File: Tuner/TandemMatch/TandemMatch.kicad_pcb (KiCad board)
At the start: 2 copper layers, 100 x 100 mm, 124 parts, among them J1 Conn_01x02, J10 Conn_01x01, J11 Conn_01x01, J12 Conn_01x01, J13 Conn_01x01, J14 Conn_01x01, J15 Conn_01x01, J16 Conn_01x01, J17 Conn_01x02, J18 Conn_Coaxial, J19 Conn_01x02, J2 Conn_01x02, J20 Conn_Coaxial, J21 Conn_01x01, J22 Conn_01x01, J23 Conn_01x01, J24 Conn_01x01, J25 Conn_01x01, J26 Conn_01x01, J27 Conn_01x01, J28 Conn_01x01, J29 Conn_01x01, J3 Conn_Coaxial, J30 Conn_01x01, J31 Conn_01x01, J32 Conn_01x01, J33 Conn_01x03, J34 Conn_01x01, J35 Conn_01x01, J36 Conn_01x01, J37 Conn_01x01, J38 Conn_01x01, J39 Conn_01x01, J4 Conn_Coaxial, J40 Conn_01x01, J41 Conn_01x01, J42 Conn_01x01, J43 Conn_01x02, J44 Conn_Coaxial, J45 Conn_01x01, J46 Conn_01x01, J47 Conn_01x01, J48 Conn_01x01, J49 Conn_01x01, J5 Conn_01x01, J50 Conn_01x01, J51 Conn_01x01, J52 Conn_01x01, J53 Conn_01x01, J54 Conn_01x02, J55 Conn_01x01, J56 Conn_01x01, J57 Conn_01x01, J58 Conn_01x02, J59 Conn_Coaxial, J6 Conn_01x01, J60 Conn_01x01, J61 Conn_01x01, J62 Conn_01x01, J63 Conn_01x01, J64 Conn_01x01, J65 Conn_01x01, J66 Conn_01x01, J67 Conn_01x01, J68 Conn_01x02, J69 Conn_01x01, J7 Conn_01x01, J70 Conn_01x01, J71 Conn_01x01, J72 Conn_01x01, J73 Conn_01x01, J74 Conn_01x02, J75 Conn_01x02, J76 Conn_01x02, J77 Conn_01x01, J78 Conn_01x01, J79 Conn_01x01, J8 Conn_01x01, J80 Conn_01x01, J81 Conn_01x01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

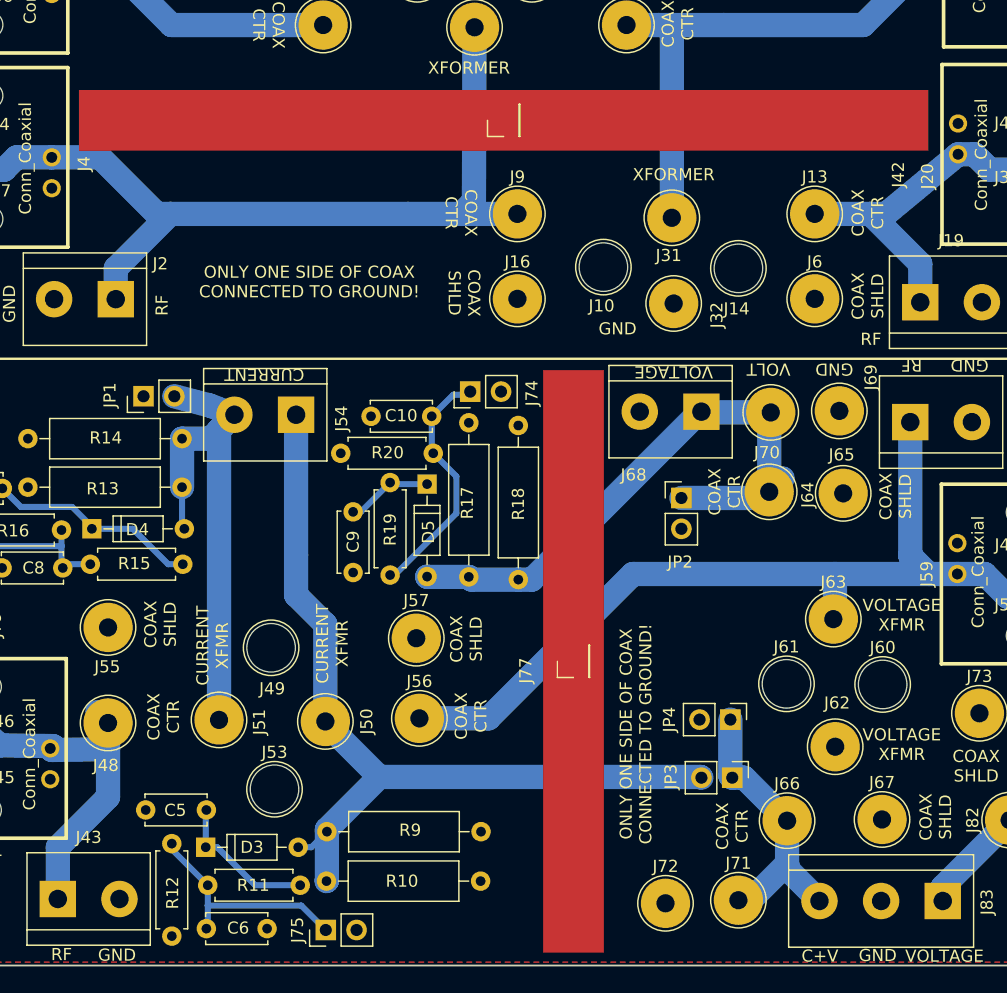
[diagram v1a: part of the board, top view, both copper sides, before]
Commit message: Fixed TandemMatch grounding problem
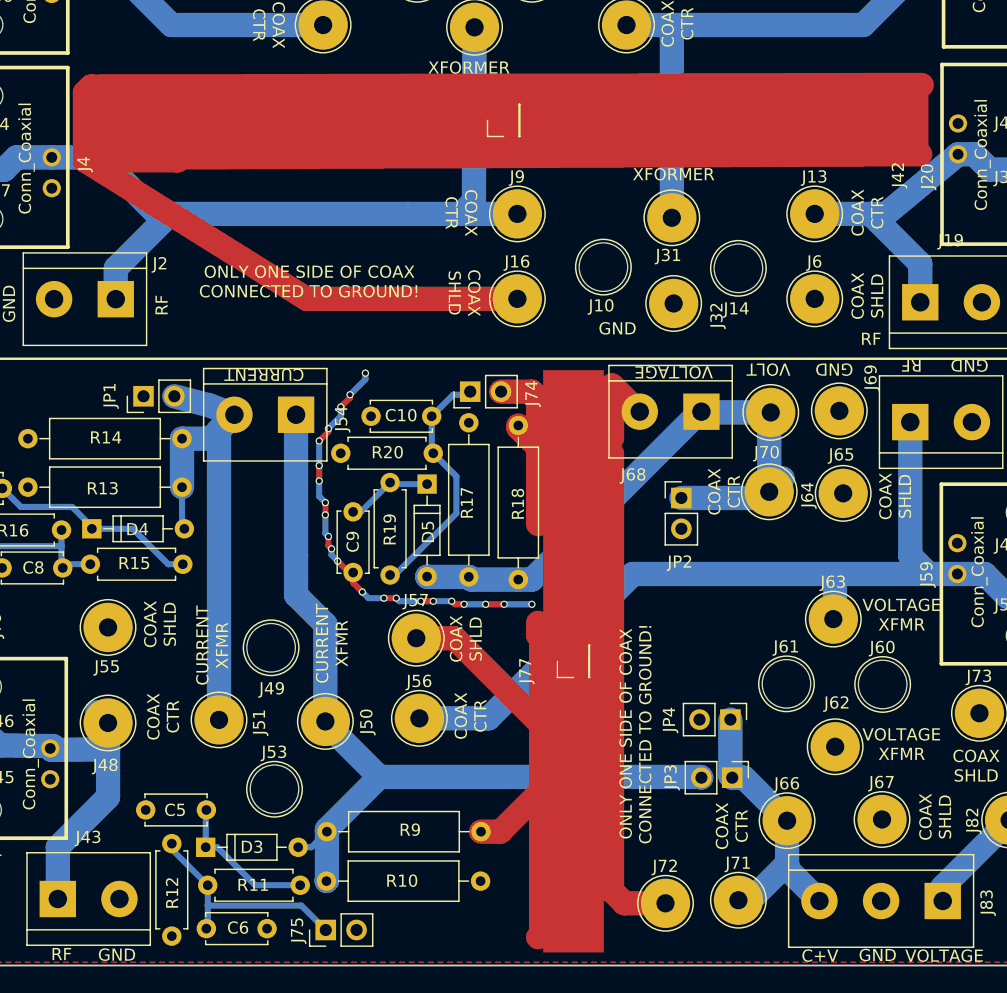
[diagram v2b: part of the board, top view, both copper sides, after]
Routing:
- net GND: track 0.00 -> 336.9 mm, vias 0 -> 22
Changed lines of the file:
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@@
     (links 149)
     (no_connects 0)
-    (area 18.581999 37.92438 161.377001 141.821259)
+    (area 39.924999 39.924999 140.075001 140.075001)
     (thickness 1.6)
     (drawings 65)
-    (tracks 204)
+    (tracks 294)
     (zones 0)
     (modules 124)
@@
   (segment (start 62.5 62.5) (end 57.404 57.404) (width 2) (layer B.Cu) (net 1))
   (segment (start 52.735 57.5) (end 52.639 57.404) (width 2) (layer B.Cu) (net 1) (status 30))
+  (segment (start 89.662 92.71) (end 92.202 92.71) (width 2) (layer F.Cu) (net 2))
+  (segment (start 92.71 93.218) (end 92.71 97.282) (width 2) (layer F.Cu) (net 2))
+  (segment (start 92.202 92.71) (end 92.71 93.218) (width 2) (layer F.Cu) (net 2))
+  (segment (start 92.71 97.282) (end 92.71 96.012) (width 2) (layer F.Cu) (net 2))
+  (segment (start 92.71 96.012) (end 92.71 97.282) (width 2) (layer F.Cu) (net 2))
+  (segment (start 101.092 94.361) (end 100.965 94.361) (width 2) (layer F.Cu) (net 2))
+  (segment (start 100.965 94.361) (end 98.806 92.202) (width 2) (layer F.Cu) (net 2))
+  (segment (start 98.806 92.202) (end 98.806 96.52) (width 2) (layer F.Cu) (net 2))
+  (segment (start 98.806 96.52) (end 98.552 96.774) (width 2) (layer F.Cu) (net 2))
+  (segment (start 82.677 113.03) (end 85.852 113.03) (width 2) (layer F.Cu) (net 2))
+  (segment (start 92.964 137.414) (end 92.71 137.668) (width 2) (layer F.Cu) (net 2))
+  (segment (start 92.964 120.142) (end 92.964 137.414) (width 2) (layer F.Cu) (net 2))
+  (segment (start 85.852 113.03) (end 92.964 120.142) (width 2) (layer F.Cu) (net 2))
+  (segment (start 91.0844 95.49892) (end 91.0844 95.6564) (width 2) (layer F.Cu) (net 2))
+  (segment (start 91.0844 95.6564) (end 92.71 97.282) (width 2) (layer F.Cu) (net 2))
+  (segment (start 92.71 97.282) (end 92.71 97.282) (width 2) (layer F.Cu) (net 2))
+  (segment (start 92.71 97.282) (end 92.71 103.632) (width 2) (layer F.Cu) (net 2))
+  (segment (start 88.011 128.97104) (end 89.60104 128.97104) (width 2) (layer F.Cu) (net 2))
+  (segment (start 92.71 112.776) (end 92.71 111.76) (width 2) (layer F.Cu) (net 2))
+  (segment (start 92.964 113.03) (end 92.71 112.776) (width 2) (layer F.Cu) (net 2))
+  (segment (start 92.964 125.60808) (end 92.964 113.03) (width 2) (layer F.Cu) (net 2))
+  (segment (start 89.60104 128.97104) (end 92.964 125.60808) (width 2) (layer F.Cu) (net 2))
+  (segment (start 103.2129 134.874) (end 99.822 134.874) (width 2) (layer F.Cu) (net 2))
+  (segment (start 98.806 133.858) (end 98.806 97.79) (width 2) (layer F.Cu) (net 2))
+  (segment (start 99.822 134.874) (end 98.806 133.858) (width 2) (layer F.Cu) (net 2))
+  (segment (start 55.372 73.66) (end 55.372 68.072) (width 2) (layer F.Cu) (net 2))
+  (segment (start 55.372 68.072) (end 55.88 67.564) (width 2) (layer F.Cu) (net 2))
+  (segment (start 55.88 67.564) (end 124.333 67.437) (width 2) (layer F.Cu) (net 2))
+  (segment (start 91.008 85.064) (end 73.634 85.064) (width 2) (layer F.Cu) (net 2))
+  (segment (start 63.246 73.406) (end 124.206 73.152) (width 2) (layer F.Cu) (net 2))
+  (segment (start 62.992 73.66) (end 63.246 73.406) (width 2) (layer F.Cu) (net 2))
+  (segment (start 55.372 73.66) (end 62.992 73.66) (width 2) (layer F.Cu) (net 2))
+  (segment (start 73.634 85.064) (end 55.372 73.66) (width 2) (layer F.Cu) (net 2))
+  (segment (start 77.47 107.616) (end 77.136 107.616) (width 0.5) (layer F.Cu) (net 2))
+  (segment (start 77.136 107.616) (end 76.2 106.68) (width 0.5) (layer F.Cu) (net 2))
+  (via (at 78.486 91.186) (size 0.6) (drill 0.4) (layers F.Cu B.Cu) (net 2))
+  (segment (start 78.486 91.694) (end 78.486 91.186) (width 0.5) (layer B.Cu) (net 2))
+  (segment (start 77.216 92.964) (end 78.486 91.694) (width 0.5) (layer B.Cu) (net 2))
+  (via (at 77.216 92.964) (size 0.6) (drill 0.4) (layers F.Cu B.Cu) (net 2))
+  (segment (start 77.216 93.218) (end 77.216 92.964) (width 0.5) (layer F.Cu) (net 2))
+  (segment (start 76.454 93.98) (end 77.216 93.218) (width 0.5) (layer F.Cu) (net 2))
+  (via (at 76.454 93.98) (size 0.6) (drill 0.4) (layers F.Cu B.Cu) (net 2))
+  (segment (start 76.454 94.742) (end 76.454 93.98) (width 0.5) (layer B.Cu) (net 2))
+  (segment (start 75.438 95.758) (end 76.454 94.742) (width 0.5) (layer B.Cu) (net 2))
+  (via (at 75.438 95.758) (size 0.6) (drill 0.4) (layers F.Cu B.Cu) (net 2))
+  (segment (start 75.438 96.012) (end 75.438 95.758) (width 0.5) (layer F.Cu) (net 2))
+  (segment (start 74.676 96.774) (end 75.438 96.012) (width 0.5) (layer F.Cu) (net 2))
+  (via (at 74.676 96.774) (size 0.6) (drill 0.4) (layers F.Cu B.Cu) (net 2))
+  (segment (start 74.676 98.806) (end 74.676 96.774) (width 0.5) (layer B.Cu) (net 2))
+  (via (at 74.676 98.806) (size 0.6) (drill 0.4) (layers F.Cu B.Cu) (net 2))
+  (segment (start 74.676 100.076) (end 74.676 98.806) (width 0.5) (layer F.Cu) (net 2))
+  (via (at 74.676 100.076) (size 0.6) (drill 0.4) (layers F.Cu B.Cu) (net 2))
+  (segment (start 74.676 101.346) (end 74.676 100.076) (width 0.5) (layer B.Cu) (net 2))
+  (segment (start 75.184 101.854) (end 74.676 101.346) (width 0.5) (layer B.Cu) (net 2))
+  (via (at 75.184 101.854) (size 0.6) (drill 0.4) (layers F.Cu B.Cu) (net 2))
+  (segment (start 75.184 102.87) (end 75.184 101.854) (width 0.5) (layer F.Cu) (net 2))
+  (via (at 75.184 102.87) (size 0.6) (drill 0.4) (layers F.Cu B.Cu) (net 2))
+  (segment (start 75.184 104.394) (end 75.184 102.87) (width 0.5) (layer B.Cu) (net 2))
+  (segment (start 75.438 104.648) (end 75.184 104.394) (width 0.5) (layer B.Cu) (net 2))
+  (via (at 75.438 104.648) (size 0.6) (drill 0.4) (layers F.Cu B.Cu) (net 2))
+  (segment (start 75.438 105.41) (end 75.438 104.648) (width 0.5) (layer F.Cu) (net 2))
+  (segment (start 75.692 105.664) (end 75.438 105.41) (width 0.5) (layer F.Cu) (net 2))
+  (via (at 75.692 105.664) (size 0.6) (drill 0.4) (layers F.Cu B.Cu) (net 2))
+  (segment (start 75.692 106.172) (end 75.692 105.664) (width 0.5) (layer B.Cu) (net 2))
+  (segment (start 76.2 106.68) (end 75.692 106.172) (width 0.5) (layer B.Cu) (net 2))
+  (via (at 76.2 106.68) (size 0.6) (drill 0.4) (layers F.Cu B.Cu) (net 2))
+  (segment (start 77.47 107.616) (end 77.47 108.458) (width 0.5) (layer F.Cu) (net 2))
+  (via (at 92.202 110.236) (size 0.6) (drill 0.4) (layers F.Cu B.Cu) (net 2))
+  (segment (start 89.916 110.236) (end 92.202 110.236) (width 0.5) (layer B.Cu) (net 2))
+  (via (at 89.916 110.236) (size 0.6) (drill 0.4) (layers F.Cu B.Cu) (net 2))
+  (segment (start 88.392 110.236) (end 89.916 110.236) (width 0.5) (layer F.Cu) (net 2))
+  (via (at 88.392 110.236) (size 0.6) (drill 0.4) (layers F.Cu B.Cu) (net 2))
+  (segment (start 86.614 110.236) (end 88.392 110.236) (width 0.5) (layer B.Cu) (net 2))
+  (via (at 86.614 110.236) (size 0.6) (drill 0.4) (layers F.Cu B.Cu) (net 2))
+  (segment (start 85.852 110.236) (end 86.614 110.236) (width 0.5) (layer F.Cu) (net 2))
+  (segment (start 85.598 109.982) (end 85.852 110.236) (width 0.5) (layer F.Cu) (net 2))
+  (via (at 85.598 109.982) (size 0.6) (drill 0.4) (layers F.Cu B.Cu) (net 2))
+  (segment (start 84.074 109.982) (end 85.598 109.982) (width 0.5) (layer B.Cu) (net 2))
+  (via (at 84.074 109.982) (size 0.6) (drill 0.4) (layers F.Cu B.Cu) (net 2))
+  (segment (start 83.058 109.982) (end 84.074 109.982) (width 0.5) (layer F.Cu) (net 2))
+  (via (at 83.058 109.982) (size 0.6) (drill 0.4) (layers F.Cu B.Cu) (net 2))
+  (segment (start 81.28 109.982) (end 83.058 109.982) (width 0.5) (layer B.Cu) (net 2))
+  (segment (start 81.026 109.728) (end 81.28 109.982) (width 0.5) (layer B.Cu) (net 2))
+  (via (at 81.026 109.728) (size 0.6) (drill 0.4) (layers F.Cu B.Cu) (net 2))
+  (segment (start 80.01 109.728) (end 81.026 109.728) (width 0.5) (layer F.Cu) (net 2))
+  (via (at 80.01 109.728) (size 0.6) (drill 0.4) (layers F.Cu B.Cu) (net 2))
+  (segment (start 78.74 109.728) (end 80.01 109.728) (width 0.5) (layer B.Cu) (net 2))
+  (segment (start 78.232 109.22) (end 78.74 109.728) (width 0.5) (layer B.Cu) (net 2))
+  (via (at 78.232 109.22) (size 0.6) (drill 0.4) (layers F.Cu B.Cu) (net 2))
+  (segment (start 77.47 108.458) (end 78.232 109.22) (width 0.5) (layer F.Cu) (net 2))
   (segment (start 87.4776 62.6872) (end 87.4268 77.0128) (width 2) (layer B.Cu) (net 3) (status 10))
   (segment (start 87.4268 77.0128) (end 86.3756 78.064) (width 2) (layer B.Cu) (net 3))

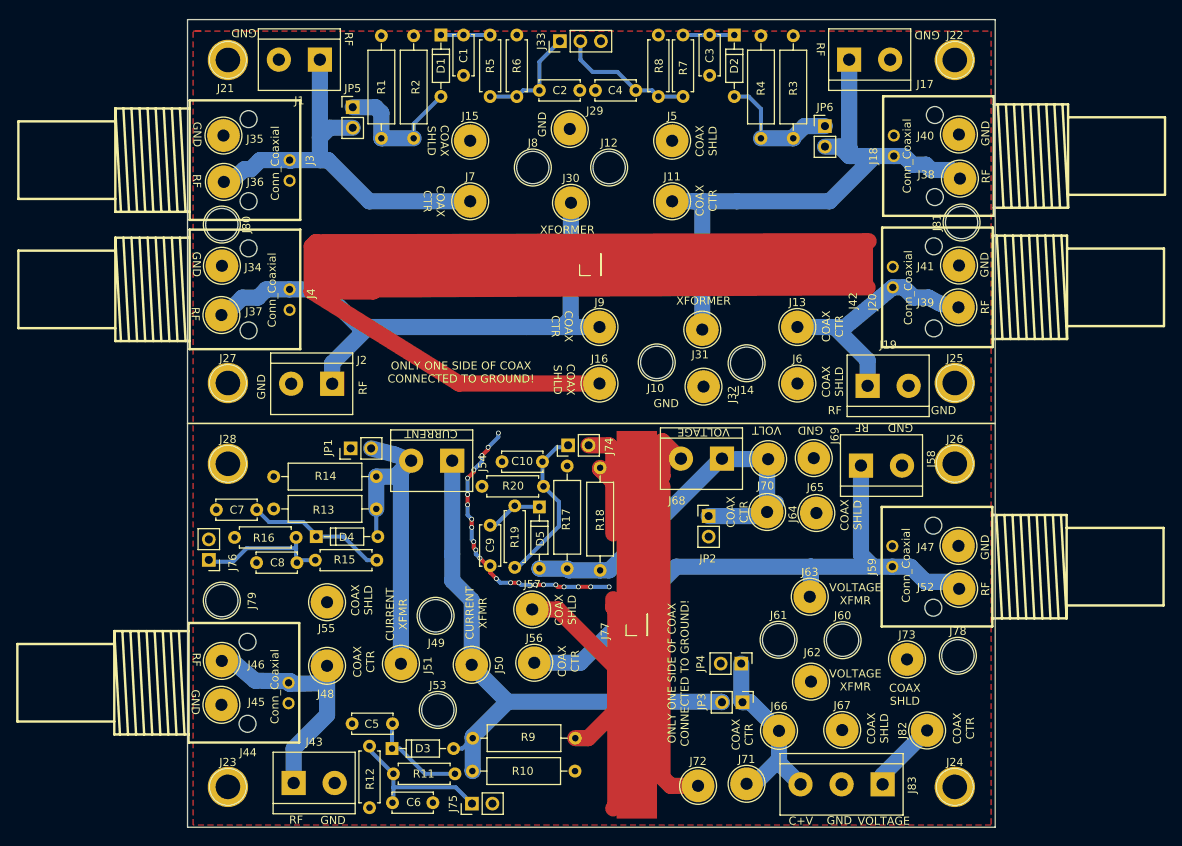
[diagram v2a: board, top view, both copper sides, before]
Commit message: Added new DelayLine board, modified TandemMatch
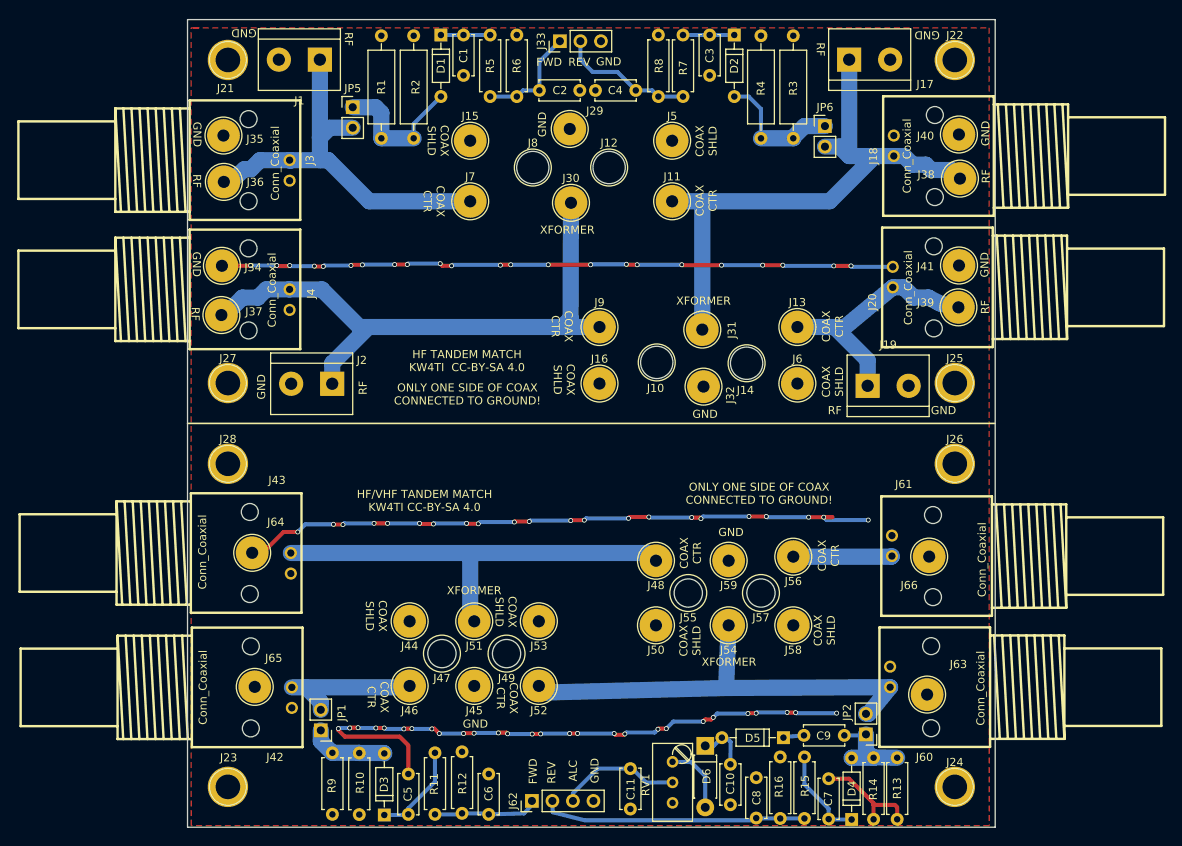
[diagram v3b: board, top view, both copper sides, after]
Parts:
- removed J67, J69, J70, J71, J72, J73, J78, J79, J80, J81, J82: Conn_01x01, Connectors:1pin
- removed J68: Conn_01x02, Connectors_Terminal_Blocks:TerminalBlock_bornier-2_P5.08mm
- removed J74, J75, J76: Conn_01x02, Pin_Headers:Pin_Header_Straight_1x02_Pitch2.54mm
- removed J77: Conn_01x01, Pin_Headers:Pin_Header_Straight_1x01_Pitch2.54mm
- removed J83: Conn_01x03, Connectors_Terminal_Blocks:TerminalBlock_bornier-3_P5.08mm
- removed JP3, JP4: Jumper_NO_Small, Pin_Headers:Pin_Header_Straight_1x02_Pitch2.54mm
- removed R17, R18: 100R, Resistors_THT:R_Axial_DIN0309_L9.0mm_D3.2mm_P12.70mm_Horizontal
- removed R19, R20: 1k, Resistors_THT:R_Axial_DIN0207_L6.3mm_D2.5mm_P7.62mm_Horizontal
- added C11: 100 nF, Capacitors_THT:C_Disc_D5.0mm_W2.5mm_P5.00mm, F.Cu at (94.8, 132.7)
- added D6: 1N4148, Diodes_THT:D_DO-41_SOD81_P7.62mm_Horizontal, F.Cu at (104.1, 129.9)
- added RV1: 10k, Potentiometers:Potentiometer_Trimmer_Bourns_3296W, F.Cu at (100.1, 131.9)
- C10: value 10 nF -> 100 nF
- J42: value Conn_01x01 -> Conn_Coaxial; footprint Pin_Headers:Pin_Header_Straight_1x01_Pitch2.54mm -> TandemMatch:bnc_90_1-1337543-0
- J43: value Conn_01x02 -> Conn_Coaxial; footprint Connectors_Terminal_Blocks:TerminalBlock_bornier-2_P5.08mm -> TandemMatch:bnc_90_1-1337543-0
- J44, J59: value Conn_Coaxial -> Conn_01x01; footprint TandemMatch:bnc_90_1-1337543-0 -> Connectors:1pin
- J54, J58: value Conn_01x02 -> Conn_01x01; footprint Connectors_Terminal_Blocks:TerminalBlock_bornier-2_P5.08mm -> Connectors:1pin
- J60, J61: value Conn_01x01 -> Conn_Coaxial; footprint Connectors:1pin -> TandemMatch:bnc_90_1-1337543-0
- J62: value Conn_01x01 -> Conn_01x04; footprint Connectors:1pin -> Pin_Headers:Pin_Header_Straight_1x04_Pitch2.54mm
- JP1, JP2: value Jumper_NO_Small -> Jumper_NC_Small
- R10, R13, R14, R9: footprint Resistors_THT:R_Axial_DIN0309_L9.0mm_D3.2mm_P12.70mm_Horizontal -> Resistors_THT:R_Axial_DIN0207_L6.3mm_D2.5mm_P7.62mm_Horizontal
- moved R13 86.2 mm to (127.9, 139.0), turned to 90 degrees
- moved R14 85.5 mm to (124.9, 139.0), turned to 90 degrees
- moved C7 80.5 mm to (119.4, 139.0), turned to 90 degrees
- moved D4 75.0 mm to (122.2, 139.0), turned to 90 degrees
- moved R16 72.8 mm to (113.4, 131.3), turned to 270 degrees
- moved J65 72.8 mm to (48.3, 122.6)
- moved J42 71.9 mm to (40.5, 122.7), turned to 270 degrees
- moved R15 68.5 mm to (116.4, 138.9), turned to 90 degrees
- moved J47 65.3 mm to (71.5, 118.5), turned to 180 degrees
- moved C8 65.1 mm to (110.4, 138.9), turned to 90 degrees
- moved J64 64.0 mm to (48.0, 106.0)
- moved J52 53.4 mm to (83.5, 122.5), turned to 180 degrees
- moved C9 46.8 mm to (116.3, 128.6), turned to 0 degrees
- moved J55 44.7 mm to (102.0, 111.0), turned to 180 degrees
- moved C10 44.1 mm to (107.2, 132.2), turned to 270 degrees
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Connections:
- C9 pad 2: GND -> Net-(C9-Pad2)
- D4 pad 2: Net-(D4-Pad2) -> Net-(C9-Pad2)
- D5 pad 2: Net-(D5-Pad2) -> Net-(C10-Pad1)
- J42 pad 1: GND -> Net-(J42-Pad1)
- J44 pad 1: Net-(J43-Pad1) -> GND
- J46 pad 1: Net-(J43-Pad1) -> Net-(J42-Pad1)
- J50 pad 1: Net-(D3-Pad2) -> GND
- J51 pad 1: Net-(D4-Pad2) -> Net-(J43-Pad1)
- J54 pad 1: Net-(D3-Pad2) -> Net-(J52-Pad1)
- J56 pad 1: Net-(J52-Pad1) -> Net-(J56-Pad1)
- J58 pad 1: Net-(J52-Pad1) -> GND
- J59 pad 1: Net-(J52-Pad1) -> GND
- J62 pad 1: GND -> Net-(C6-Pad1)
- J63 pad 1: Net-(J52-Pad1) -> GND
- J64 pad 1: Net-(D5-Pad2) -> GND
- J66 pad 1: Net-(J66-Pad1) -> GND
- JP1 pad 1: GND -> Net-(D3-Pad2)
- JP1 pad 2: Net-(D4-Pad2) -> Net-(J42-Pad1)
- JP2 pad 1: Net-(D5-Pad2) -> Net-(C9-Pad2)
- JP2 pad 2: GND -> Net-(J52-Pad1)
- R13 pad 2: Net-(D4-Pad2) -> Net-(C9-Pad2)
- R14 pad 2: Net-(D4-Pad2) -> Net-(C9-Pad2)
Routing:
- net GND: track 336.9 -> 254.5 mm, vias 22 -> 73
- net Net-(D3-Pad2): track 72.5 -> 9.84 mm
- net Net-(D5-Pad2): track 50.0 -> 0.00 mm
- net Net-(D4-Pad2): track 41.7 -> 0.00 mm
- net Net-(J66-Pad1): track 23.9 -> 0.00 mm
- net Net-(J43-Pad1): track 32.0 -> 54.3 mm
- net Net-(J52-Pad1): track 75.6 -> 56.2 mm
- net Net-(J42-Pad1): track 0.00 -> 17.3 mm
- net Net-(C11-Pad1): track 0.00 -> 15.7 mm
- net Net-(C8-Pad1): track 17.2 -> 32.8 mm
- net Net-(C10-Pad1): track 20.4 -> 6.54 mm
- net Net-(J56-Pad1): track 0.00 -> 12.2 mm
- net Net-(C9-Pad2): track 0.00 -> 11.7 mm
- net Net-(J82-Pad1): track 8.95 -> 0.00 mm
- net Net-(D6-Pad2): track 0.00 -> 8.65 mm
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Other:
- board text added: "ALC"
- board text added: "FWD"
- board text added: "HF TANDEM MATCH KW4TI CC-BY-SA 4.0"
- board text added: "HF/VHF TANDEM MATCH KW4TI CC-BY-SA 4.0"
- board text added: "REV"
- board text removed: "C+V"
- board text removed: "CURRENT"
- board text removed: "CURRENT XFMR"
- board text removed: "VOLT"
- board text removed: "VOLTAGE"
- board text removed: "VOLTAGE XFMR"
